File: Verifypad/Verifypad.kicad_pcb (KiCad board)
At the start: 2 copper layers, 46 x 42.5 mm, 4 parts, among them SW1 SW_Push, SW2 SW_Push, U1 MOUDLE-SEEEDUINO-XIAO

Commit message: Kicad
new kicad stuff :)
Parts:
- added J1: Conn_01x04, Connector_PinHeader_2.54mm:PinHeader_1x04_P2.54mm_Vertical, F.Cu at (192.3, 72.6)
- added REF**: MountingHole_2.5mm, MountingHole:MountingHole_2.5mm, F.Cu at (164.2, 51.0)
- added REF**: MountingHole_2.5mm, MountingHole:MountingHole_2.5mm, F.Cu at (164.2, 95.3)
- added REF**: MountingHole_2.5mm, MountingHole:MountingHole_2.5mm, F.Cu at (205.8, 51.0)
- added REF**: 0.49Display, Verifypad:0.49Display, F.Cu at (193.6, 63.2)
- added REF**: MountingHole_2.5mm, MountingHole:MountingHole_2.5mm, F.Cu at (205.9, 95.3)
- G***: moved to B.Cu
- moved U1 54.0 mm to (175.5, 63.8)
- moved SW2 50.7 mm to (195.8, 84.5)
- moved G*** 48.6 mm to (175.7, 92.2), turned to 180 degrees
- moved SW1 26.1 mm to (175.6, 84.4)
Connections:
- U1 pad 14: unconnected-(U1-5V-Pad14)_1 -> /VCC
- U1 pad 6: unconnected-(U1-PA9_A5_D5_SCL-Pad6)_1 -> /I2CD
- U1 pad 7: unconnected-(U1-PB08_A6_D6_TX-Pad7)_1 -> /I2CC
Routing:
- net /I2CD: track 0.00 -> 28.5 mm
- net /I2CC: track 0.00 -> 24.9 mm
- net /VCC: track 0.00 -> 24.3 mm
- net GND: track 38.1 -> 52.8 mm
- net Net-(U1-PA5_A9_D9_MISO): track 14.5 -> 26.4 mm, vias 0 -> 2
- net Net-(U1-PA7_A8_D8_SCK): track 14.6 -> 25.7 mm
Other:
- board size 46 x 42.5 mm -> 48.9 x 53.6 mm
- board text added: "VerifyPad"

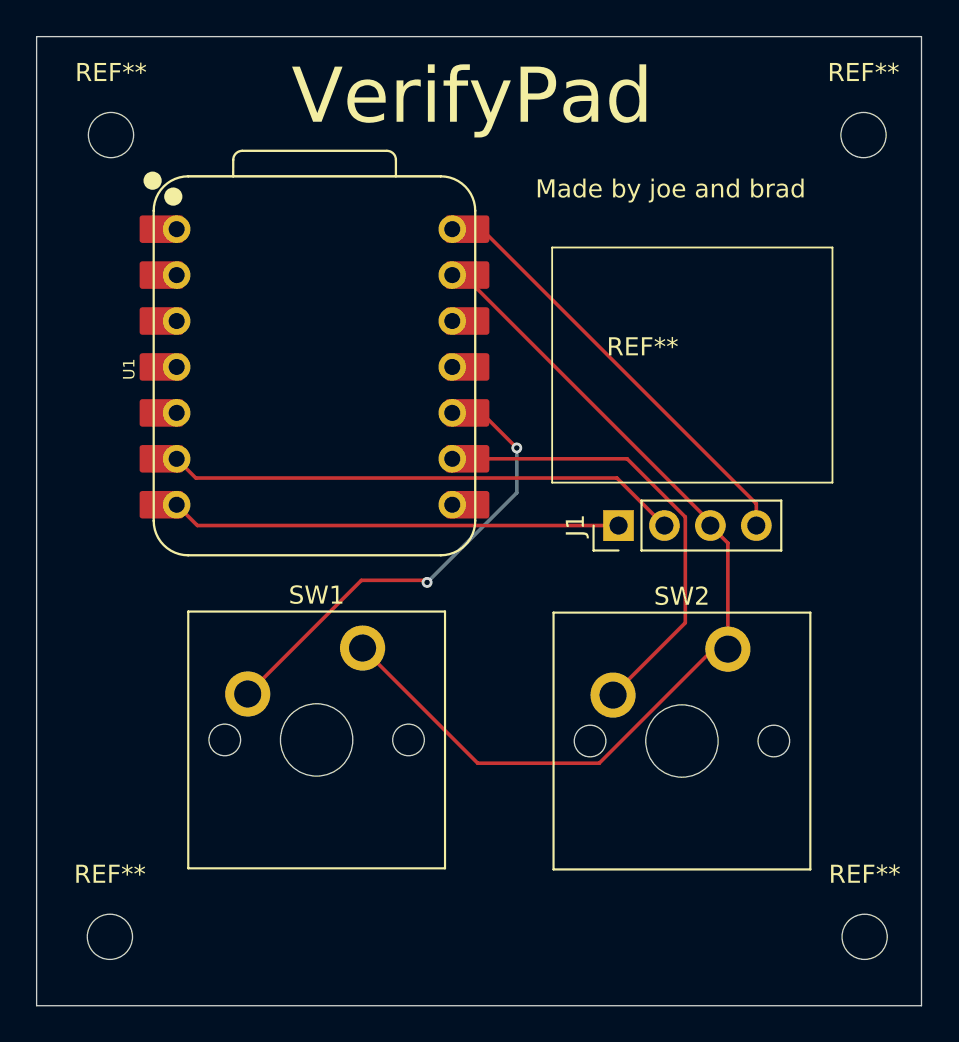
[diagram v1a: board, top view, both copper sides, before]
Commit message: changed sizing and got STL
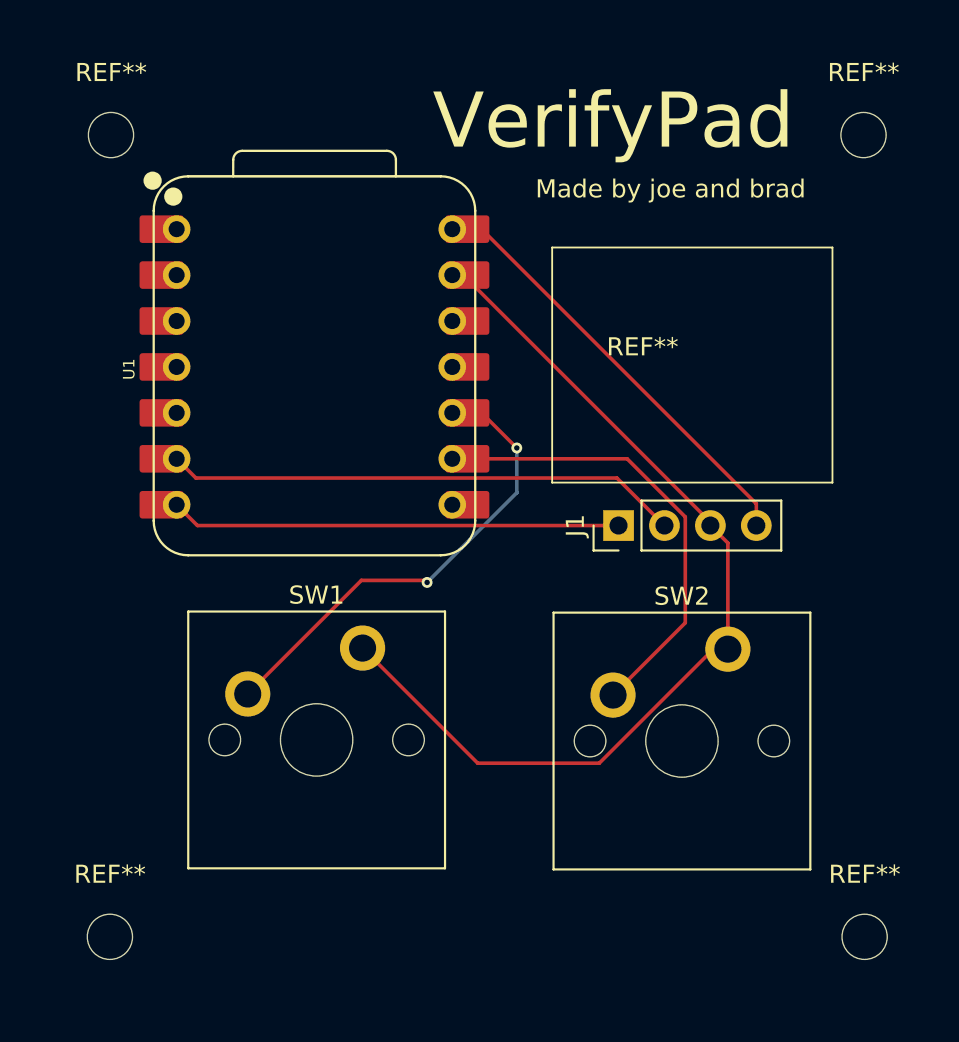
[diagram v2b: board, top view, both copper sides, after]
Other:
- board outline removed

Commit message: PCbbbbadsadldj
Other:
- board outline added: 49 x 51.5 mm
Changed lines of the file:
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@@
 			)
 		)
-		(property "Datasheet" "~"
+		(property "Datasheet" ""
 			(at 0 0 90)
 			(layer "F.Fab")
@@
 		(sheetname "/")
 		(sheetfile "Verifypad.kicad_sch")
+		(units
+			(unit
+				(name "A")
+				(pins "1" "2" "3" "4")
+			)
+		)
 		(attr through_hole)
 		(duplicate_pad_numbers_are_jumpers no)
@@
 			(remove_unused_layers no)
 			(net "/I2CC")
-			(pinfunction "Pin_1")
+			(pinfunction "Pin_1_1")
 			(pintype "passive")
 		)
@@
 			(remove_unused_layers no)
 			(net "/I2CD")
-			(pinfunction "Pin_2")
+			(pinfunction "Pin_2_2")
 			(pintype "passive")
 		)
@@
 			(remove_unused_layers no)
 			(net "GND")
-			(pinfunction "Pin_3")
+			(pinfunction "Pin_3_3")
 			(pintype "passive")
 		)
@@
 			(remove_unused_layers no)
 			(net "/VCC")
-			(pinfunction "Pin_4")
+			(pinfunction "Pin_4_4")
 			(pintype "passive")
 		)
@@
 			)
 		)
-		(property "Datasheet" "~"
+		(property "Datasheet" ""
 			(at 0 0 0)
 			(layer "F.Fab")
@@
 		(sheetname "/")
 		(sheetfile "Verifypad.kicad_sch")
+		(units
+			(unit
+				(name "A")
+				(pins "1" "2")
+			)
+		)
 		(attr through_hole)
 		(duplicate_pad_numbers_are_jumpers no)
@@
 			(remove_unused_layers no)
 			(net "Net-(U1-PA7_A8_D8_SCK)")
-			(pinfunction "1")
+			(pinfunction "1_1")
 			(pintype "passive")
 		)
@@
 			(remove_unused_layers no)
 			(net "GND")
-			(pinfunction "2")
+			(pinfunction "2_2")
 			(pintype "passive")
 		)
@@
 		(sheetname "/")
 		(sheetfile "Verifypad.kicad_sch")
+		(units
+			(unit
+				(name "A")
+				(pins "1" "2" "3" "4" "5" "6" "7" "14" "13" "12" "11" "10" "9" "8")
+			)
+		)
 		(attr smd)
 		(duplicate_pad_numbers_are_jumpers no)
@@
 			(roundrect_rratio 0.1)
 			(net "unconnected-(U1-PA02_A0_D0-Pad1)_1")
-			(pinfunction "PA02_A0_D0")
+			(pinfunction "PA02_A0_D0_1")
 			(pintype "passive+no_connect")
 			(thermal_bridge_angle 45)
@@
 			(remove_unused_layers no)
 			(net "unconnected-(U1-PA02_A0_D0-Pad1)")
-			(pinfunction "PA02_A0_D0")
+			(pinfunction "PA02_A0_D0_1")
 			(pintype "passive+no_connect")
 		)
@@
 			(roundrect_rratio 0.1)
 			(net "unconnected-(U1-PA4_A1_D1-Pad2)")
-			(pinfunction "PA4_A1_D1")
+			(pinfunction "PA4_A1_D1_2")
 			(pintype "passive+no_connect")
 			(thermal_bridge_angle 45)
@@
 			(remove_unused_layers no)
 			(net "unconnected-(U1-PA4_A1_D1-Pad2)_1")
-			(pinfunction "PA4_A1_D1")
+			(pinfunction "PA4_A1_D1_2")
 			(pintype "passive+no_connect")
 		)
@@
 			(roundrect_rratio 0.1)
 			(net "unconnected-(U1-PA10_A2_D2-Pad3)")
-			(pinfunction "PA10_A2_D2")
+			(pinfunction "PA10_A2_D2_3")
 			(pintype "passive+no_connect")
 			(thermal_bridge_angle 45)
@@
 			(remove_unused_layers no)
 			(net "unconnected-(U1-PA10_A2_D2-Pad3)_1")
-			(pinfunction "PA10_A2_D2")
+			(pinfunction "PA10_A2_D2_3")
 			(pintype "passive+no_connect")
 		)
@@
 			(roundrect_rratio 0.1)
 			(net "unconnected-(U1-PA11_A3_D3-Pad4)")
-			(pinfunction "PA11_A3_D3")
+			(pinfunction "PA11_A3_D3_4")
 			(pintype "passive+no_connect")
 			(thermal_bridge_angle 45)
@@
 			(remove_unused_layers no)
 			(net "unconnected-(U1-PA11_A3_D3-Pad4)_1")
-			(pinfunction "PA11_A3_D3")
+			(pinfunction "PA11_A3_D3_4")
 			(pintype "passive+no_connect")
 		)
@@
 			(roundrect_rratio 0.1)
 			(net "unconnected-(U1-PA8_A4_D4_SDA-Pad5)_1")
-			(pinfunction "PA8_A4_D4_SDA")
+			(pinfunction "PA8_A4_D4_SDA_5")
 			(pintype "passive+no_connect")
 			(thermal_bridge_angle 45)
@@
 			(remove_unused_layers no)
 			(net "unconnected-(U1-PA8_A4_D4_SDA-Pad5)")
-			(pinfunction "PA8_A4_D4_SDA")
+			(pinfunction "PA8_A4_D4_SDA_5")
 			(pintype "passive+no_connect")
 		)
@@
 			(roundrect_rratio 0.1)
 			(net "/I2CD")
-			(pinfunction "PA9_A5_D5_SCL")
+			(pinfunction "PA9_A5_D5_SCL_6")
 			(pintype "passive")
 			(thermal_bridge_angle 45)
@@
 			(remove_unused_layers no)
 			(net "/I2CD")
-			(pinfunction "PA9_A5_D5_SCL")
+			(pinfunction "PA9_A5_D5_SCL_6")
 			(pintype "passive")
 		)
@@
 			(roundrect_rratio 0.1)
 			(net "/I2CC")
-			(pinfunction "PB08_A6_D6_TX")
+			(pinfunction "PB08_A6_D6_TX_7")
 			(pintype "passive")
 			(thermal_bridge_angle 45)
@@
 			(remove_unused_layers no)
 			(net "/I2CC")
-			(pinfunction "PB08_A6_D6_TX")
+			(pinfunction "PB08_A6_D6_TX_7")
 			(pintype "passive")
 		)
@@
 			(remove_unused_layers no)
 			(net "unconnected-(U1-PB09_A7_D7_RX-Pad8)")
-			(pinfunction "PB09_A7_D7_RX")
+			(pinfunction "PB09_A7_D7_RX_8")
 			(pintype "passive+no_connect")
 		)
@@
 			(roundrect_rratio 0.1)
 			(net "unconnected-(U1-PB09_A7_D7_RX-Pad8)_1")
-			(pinfunction "PB09_A7_D7_RX")
+			(pinfunction "PB09_A7_D7_RX_8")
 			(pintype "passive+no_connect")
 			(thermal_bridge_angle 45)
@@
 			(remove_unused_layers no)
 			(net "Net-(U1-PA7_A8_D8_SCK)")
-			(pinfunction "PA7_A8_D8_SCK")
+			(pinfunction "PA7_A8_D8_SCK_9")
 			(pintype "passive")
 		)
@@
 			(roundrect_rratio 0.1)
 			(net "Net-(U1-PA7_A8_D8_SCK)")
-			(pinfunction "PA7_A8_D8_SCK")
+			(pinfunction "PA7_A8_D8_SCK_9")
 			(pintype "passive")
 			(thermal_bridge_angle 45)
@@
 			(remove_unused_layers no)
 			(net "Net-(U1-PA5_A9_D9_MISO)")
-			(pinfunction "PA5_A9_D9_MISO")
+			(pinfunction "PA5_A9_D9_MISO_10")
 			(pintype "passive")
 		)
@@
 			(roundrect_rratio 0.1)
 			(net "Net-(U1-PA5_A9_D9_MISO)")
-			(pinfunction "PA5_A9_D9_MISO")
+			(pinfunction "PA5_A9_D9_MISO_10")
 			(pintype "passive")
 			(thermal_bridge_angle 45)
@@
 			(remove_unused_layers no)
 			(net "unconnected-(U1-PA6_A10_D10_MOSI-Pad11)_1")
-			(pinfunction "PA6_A10_D10_MOSI")
+			(pinfunction "PA6_A10_D10_MOSI_11")
 			(pintype "passive+no_connect")
 		)
@@
 			(roundrect_rratio 0.1)
 			(net "unconnected-(U1-PA6_A10_D10_MOSI-Pad11)")
-			(pinfunction "PA6_A10_D10_MOSI")
+			(pinfunction "PA6_A10_D10_MOSI_11")
 			(pintype "passive+no_connect")
 			(thermal_bridge_angle 45)
@@
 			(remove_unused_layers no)
 			(net "unconnected-(U1-3V3-Pad12)")
-			(pinfunction "3V3")
+			(pinfunction "3V3_12")
 			(pintype "passive+no_connect")
 		)
@@
 			(roundrect_rratio 0.1)
 			(net "unconnected-(U1-3V3-Pad12)_1")
-			(pinfunction "3V3")
+			(pinfunction "3V3_12")
 			(pintype "passive+no_connect")
 			(thermal_bridge_angle 45)
@@
 			(remove_unused_layers no)
 			(net "GND")
-			(pinfunction "GND")
+			(pinfunction "GND_13")
 			(pintype "passive")
 		)
@@
 			(roundrect_rratio 0.1)
 			(net "GND")
-			(pinfunction "GND")
+			(pinfunction "GND_13")
 			(pintype "passive")
 			(thermal_bridge_angle 45)
@@
 			(remove_unused_layers no)
 			(net "/VCC")
-			(pinfunction "5V")
+			(pinfunction "5V_14")
 			(pintype "passive")
 		)
@@
 			(roundrect_rratio 0.1)
 			(net "/VCC")
-			(pinfunction "5V")
+			(pinfunction "5V_14")
 			(pintype "passive")
 			(thermal_bridge_angle 45)
@@
 			)
 		)
+		(model "C:/Users/Joe/Downloads/seeed-studio-xiao-rp2040-3d-model/Seeed Studio XIAO RP2040 v26.step"
+			(offset
+				(xyz 0 0 0)
+			)
+			(scale
+				(xyz 1 1 1)
+			)
+			(rotate
+				(xyz -0 -0 90)
+			)
+		)
 	)
 	(footprint "Verifypad:0.49Display"
@@
 			)
 		)
-		(property "Datasheet" "~"
+		(property "Datasheet" ""
 			(at 0 0 0)
 			(layer "F.Fab")
@@
 		(sheetname "/")
 		(sheetfile "Verifypad.kicad_sch")
+		(units
+			(unit
+				(name "A")
+				(pins "1" "2")
+			)
+		)
 		(attr through_hole)
 		(duplicate_pad_numbers_are_jumpers no)
@@
 			(remove_unused_layers no)
 			(net "Net-(U1-PA5_A9_D9_MISO)")
-			(pinfunction "1")
+			(pinfunction "1_1")
 			(pintype "passive")
 		)
@@
 			(remove_unused_layers no)
 			(net "GND")
-			(pinfunction "2")
+			(pinfunction "2_2")
 			(pintype "passive")
 		)
@@
 		(stroke
 			(width 0.1)
-			(type default)
+			(type solid)
 		)
 		(fill no)
-		(layer "B.SilkS")
+		(layer "Edge.Cuts")
 	)
 	(gr_text "Made by joe and brad"
@@
 	)
 	(segment
+		(start 168.99492 72.5808)
+		(end 192.279128 72.5808)
+		(width 0.2)
+		(layer "F.Cu")
+		(net "/I2CC")
+	)
+	(segment
+		(start 167.845068 71.430948)
+		(end 168.99492 72.5808)
+		(width 0.2)
+		(layer "F.Cu")
+		(net "/I2CC")
+	)
+	(segment
 		(start 167.845068 68.890948)
 		(end 168.908068 69.953948)
@@
 	)
 	(segment
-		(start 168.99492 72.5808)
-		(end 192.279128 72.5808)
-		(width 0.2)
-		(layer "F.Cu")
-		(net "/I2CC")
-	)
-	(segment
-		(start 167.845068 71.430948)
-		(end 168.99492 72.5808)
-		(width 0.2)
-		(layer "F.Cu")
-		(net "/I2CC")
-	)
-	(segment
 		(start 199.899128 72.5808)
 		(end 199.899128 71.378719)
@@
 	)
 	(segment
+		(start 191.976052 81.956148)
+		(end 195.970128 77.962072)
+		(width 0.2)
+		(layer "F.Cu")
+		(net "Net-(U1-PA7_A8_D8_SCK)")
+	)
+	(segment
+		(start 195.970128 72.10404)
+		(end 192.757036 68.890948)
+		(width 0.2)
+		(layer "F.Cu")
+		(net "Net-(U1-PA7_A8_D8_SCK)")
+	)
+	(segment
+		(start 195.970128 77.962072)
+		(end 195.970128 72.10404)
+		(width 0.2)
+		(layer "F.Cu")
+		(net "Net-(U1-PA7_A8_D8_SCK)")
+	)
+	(segment
+		(start 192.757036 68.890948)
+		(end 183.085068 68.890948)
+		(width 0.2)
+		(layer "F.Cu")
+		(net "Net-(U1-PA7_A8_D8_SCK)")
+	)
+	(segment
 		(start 186.653624 68.290948)
 		(end 184.713624 66.350948)
@@
 		(net "Net-(U1-PA5_A9_D9_MISO)")
 	)
-	(segment
-		(start 191.976052 81.956148)
-		(end 195.970128 77.962072)
-		(width 0.2)
-		(layer "F.Cu")
-		(net "Net-(U1-PA7_A8_D8_SCK)")
-	)
-	(segment
-		(start 195.970128 72.10404)
-		(end 192.757036 68.890948)
-		(width 0.2)
-		(layer "F.Cu")
-		(net "Net-(U1-PA7_A8_D8_SCK)")
-	)
-	(segment
-		(start 195.970128 77.962072)
-		(end 195.970128 72.10404)
-		(width 0.2)
-		(layer "F.Cu")
-		(net "Net-(U1-PA7_A8_D8_SCK)")
-	)
-	(segment
-		(start 192.757036 68.890948)
-		(end 183.085068 68.890948)
-		(width 0.2)
-		(layer "F.Cu")
-		(net "Net-(U1-PA7_A8_D8_SCK)")
-	)
 	(embedded_fonts no)
